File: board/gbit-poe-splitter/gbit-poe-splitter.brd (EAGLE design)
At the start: 61.3 x 42.2 mm, 51 parts, among them IC1 LM2596HVS, U1 TPS2379DDA

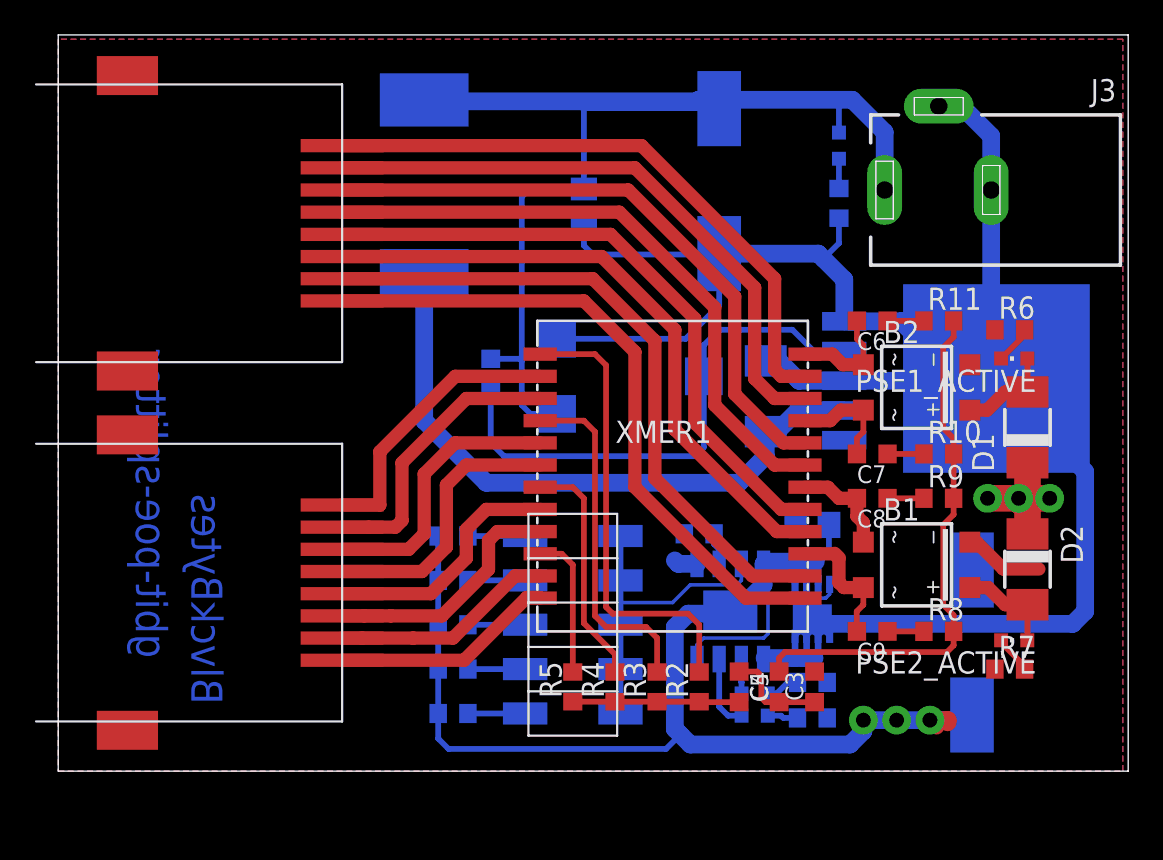
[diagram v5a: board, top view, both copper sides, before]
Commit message: Fixed horrible ethernet pin swap
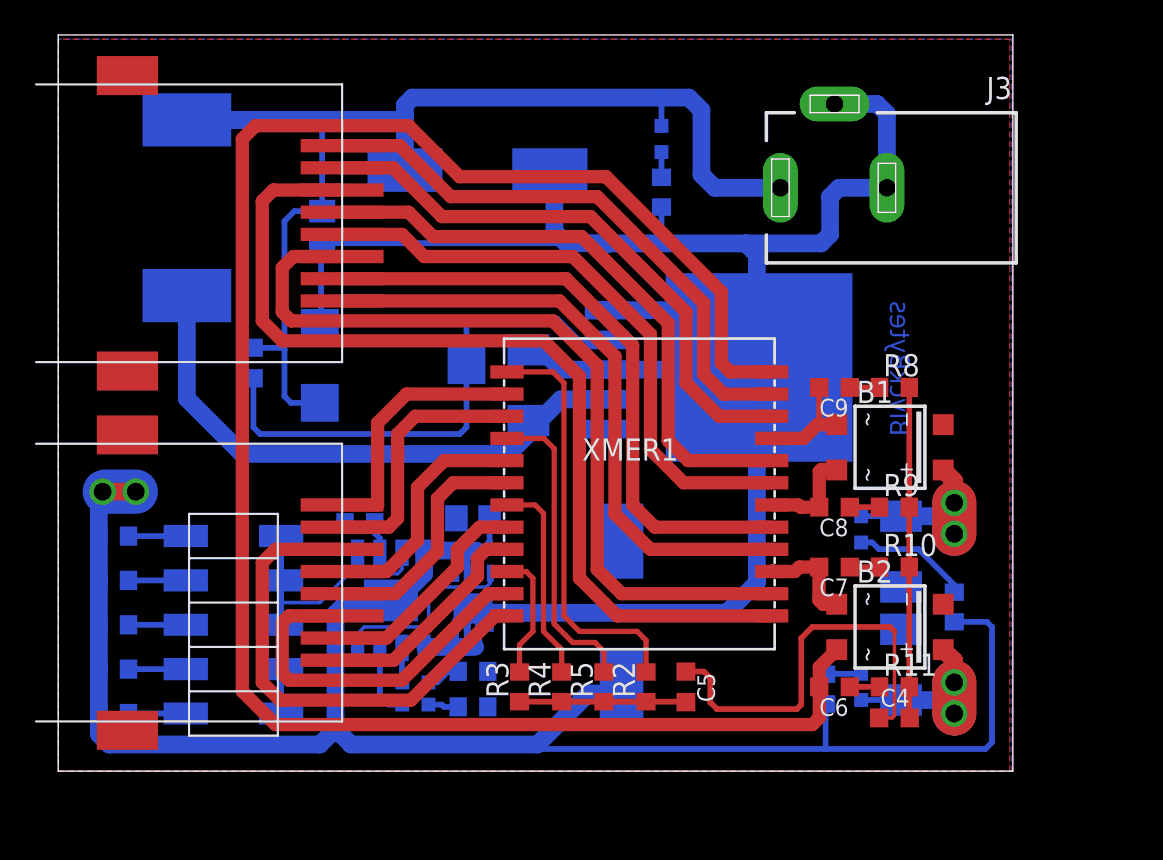
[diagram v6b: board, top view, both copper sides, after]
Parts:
- removed C3: 1nF, rcl:C0603K
- moved R6 23.1 mm to (43.9, 11.0), flipped to the bottom, turned to 90 degrees
- moved R11 21.1 mm to (47.9, 11.2)
- moved C6 21.1 mm to (44.5, 11.2)
- moved PSE1_ACTIVE 20.7 mm to (46.0, 11.2), flipped to the bottom, turned to 0 degrees
- moved C12 20.1 mm to (32.3, 15.4)
- moved R19 19.4 mm to (17.3, 20.6)
- moved U1 19.4 mm to (19.1, 16.1)
- moved INRUSH_LIMITED 19.4 mm to (20.4, 11.4)
- moved R12 19.4 mm to (23.7, 10.0)
- moved R13 19.4 mm to (23.7, 12.1)
- moved TYPE2_PSE 19.4 mm to (20.4, 10.2)
- moved U$1 19.4 mm to (23.7, 16.3)
- moved C10 19.4 mm to (23.7, 20.8)
- moved R1 19.4 mm to (3.17, 9.65)
- moved R15 19.4 mm to (3.17, 12.2)
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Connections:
- removed net N$17: C3.1, C4.1, C5.1
- net GND: now also C4.1, C5.1; no longer C3.2
- net N$10: now also ETH-IN.P4, XMER1.20; no longer ETH-IN.P7, XMER1.14
- net N$11: now also ETH-IN.P8; no longer ETH-IN.P6
- net N$12: now also XMER1.19; no longer XMER1.17
- net N$13: now also ETH-IN.P6, XMER1.14; no longer ETH-IN.P4, XMER1.19
- net N$14: now also XMER1.13; no longer XMER1.20
- net N$3: now also XMER1.12; no longer XMER1.5
- net N$4: now also XMER1.5; no longer XMER1.6
- net N$5: now also XMER1.6; no longer XMER1.8
- net N$6: now also XMER1.11; no longer XMER1.9
- net N$7: now also XMER1.8; no longer XMER1.11
- net N$8: now also XMER1.9; no longer XMER1.12
- net N$9: now also ETH-IN.P7, XMER1.17; no longer ETH-IN.P8, XMER1.13
- net PD1B: now also XMER1.10; no longer XMER1.4
- net PD2B: now also XMER1.4; no longer XMER1.10
- net PSE1A: now also B2.~2; no longer B2.~1
- net PSE1B: now also B2.~1, XMER1.15; no longer B2.~2, XMER1.21
- net PSE2A: now also B1.~2; no longer B1.~1
- net PSE2B: now also B1.~1, XMER1.21; no longer B1.~2, XMER1.15
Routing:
- net PSE1A: track 6.25 -> 108.8 mm
- net GND: track 73.5 -> 134.8 mm, vias 3 -> 2
- net N$14: track 35.8 -> 54.6 mm
- net PSE: track 17.5 -> 0.00 mm, vias 3 -> 0
- net PD1B: track 20.0 -> 7.33 mm
- net N$3: track 15.9 -> 28.2 mm
- net N$13: track 35.8 -> 47.8 mm
- net N$19: track 30.6 -> 18.9 mm
- net POWER: track 66.4 -> 76.1 mm
- net PD2B: track 8.26 -> 17.7 mm
- net N$6: track 14.3 -> 21.6 mm
- net PSE1: track 5.65 -> 11.4 mm, vias 0 -> 2
- net N$17: track 5.79 -> 0.00 mm
- net PSE2: track 5.75 -> 11.3 mm, vias 0 -> 2
- net N$25: track 2.93 -> 6.76 mm
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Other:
- board size 61.3 x 42.2 mm -> 54.7 x 42.2 mm
- board text removed: "gbit-poe-splitter"
